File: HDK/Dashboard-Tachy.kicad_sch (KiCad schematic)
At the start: 54 parts, among them J101 Conn_02x08_Odd_Even, U101 CA56-12CGKWA

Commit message: updated rev1.1
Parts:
- H101, H102, H103, H104: footprint MountingHole:MountingHole_3.2mm_M3_DIN965_Pad_TopBottom -> MountingHole:MountingHole_4.3mm_M4_DIN965_Pad_TopBottom

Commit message: updated REV1.1
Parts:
- C101, C102, C103, C104, C105, C106, C107, C108, C109, C110, C111, C112, C113, C114, C115, C116, C117, C118, C119, C120, C121, C122, C123, C124: footprint Capacitor_SMD:C_0402_1005Metric -> Capacitor_SMD:C_0603_1608Metric; LCSC (none) -> C14663
- D101, D102, D103, D104, D105, D106, D107, D108, D109, D110, D111, D112, D113, D114, D115, D116, D117, D118, D119, D120, D121, D122, D123, D124: LCSC (none) -> C2761795

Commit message: added fab
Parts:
- D101, D102, D103, D104, D105, D106, D107, D108, D109, D110, D111, D112, D113, D114, D115, D116, D117, D118, D119, D120, D121, D122, D123, D124: LCSC C2761795 -> C2843785
- H101, H102, H103, H104: LCSC (none) -> -; now left out of the parts list
- J101: footprint Connector_JST:JST_PHD_B16B-PHDSS_2x08_P2.00mm_Vertical -> NVF-Kicad:PHD_02x08V-H; LCSC (none) -> -
- U101: LCSC (none) -> -

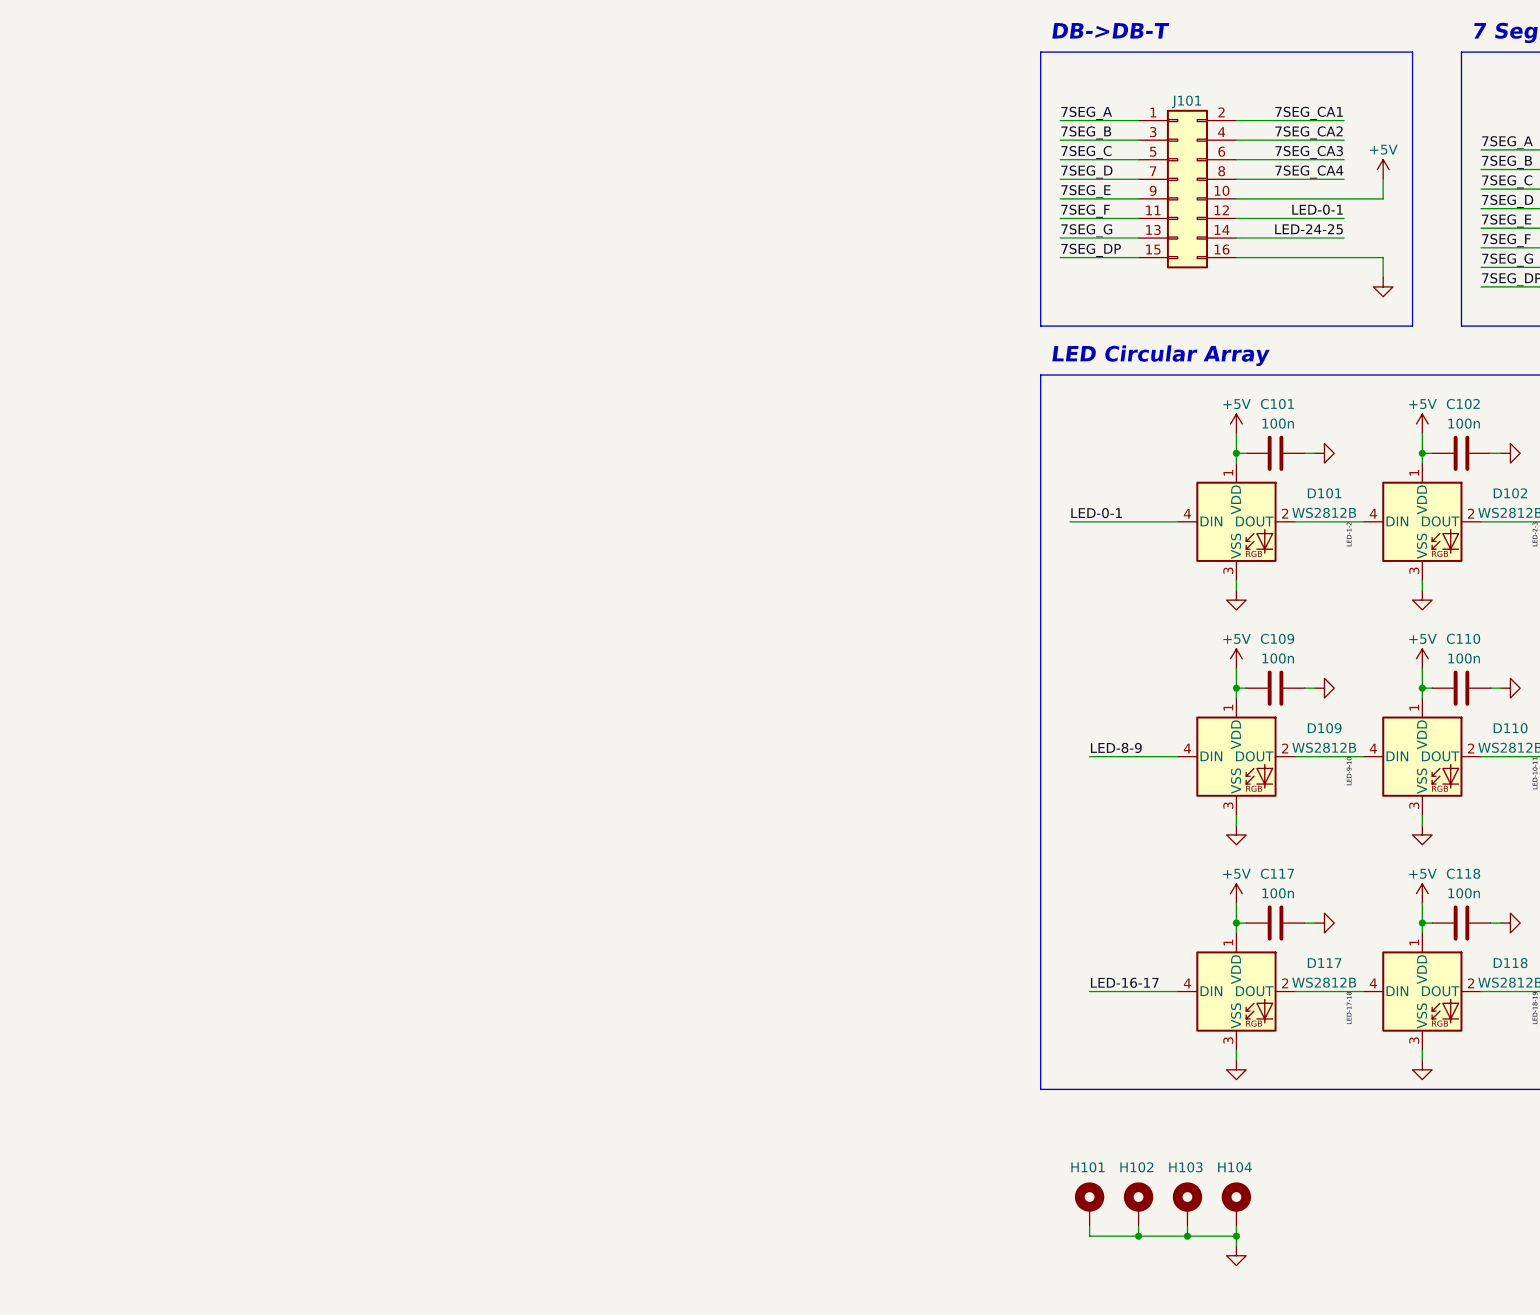
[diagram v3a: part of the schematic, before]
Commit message: updated dimensions
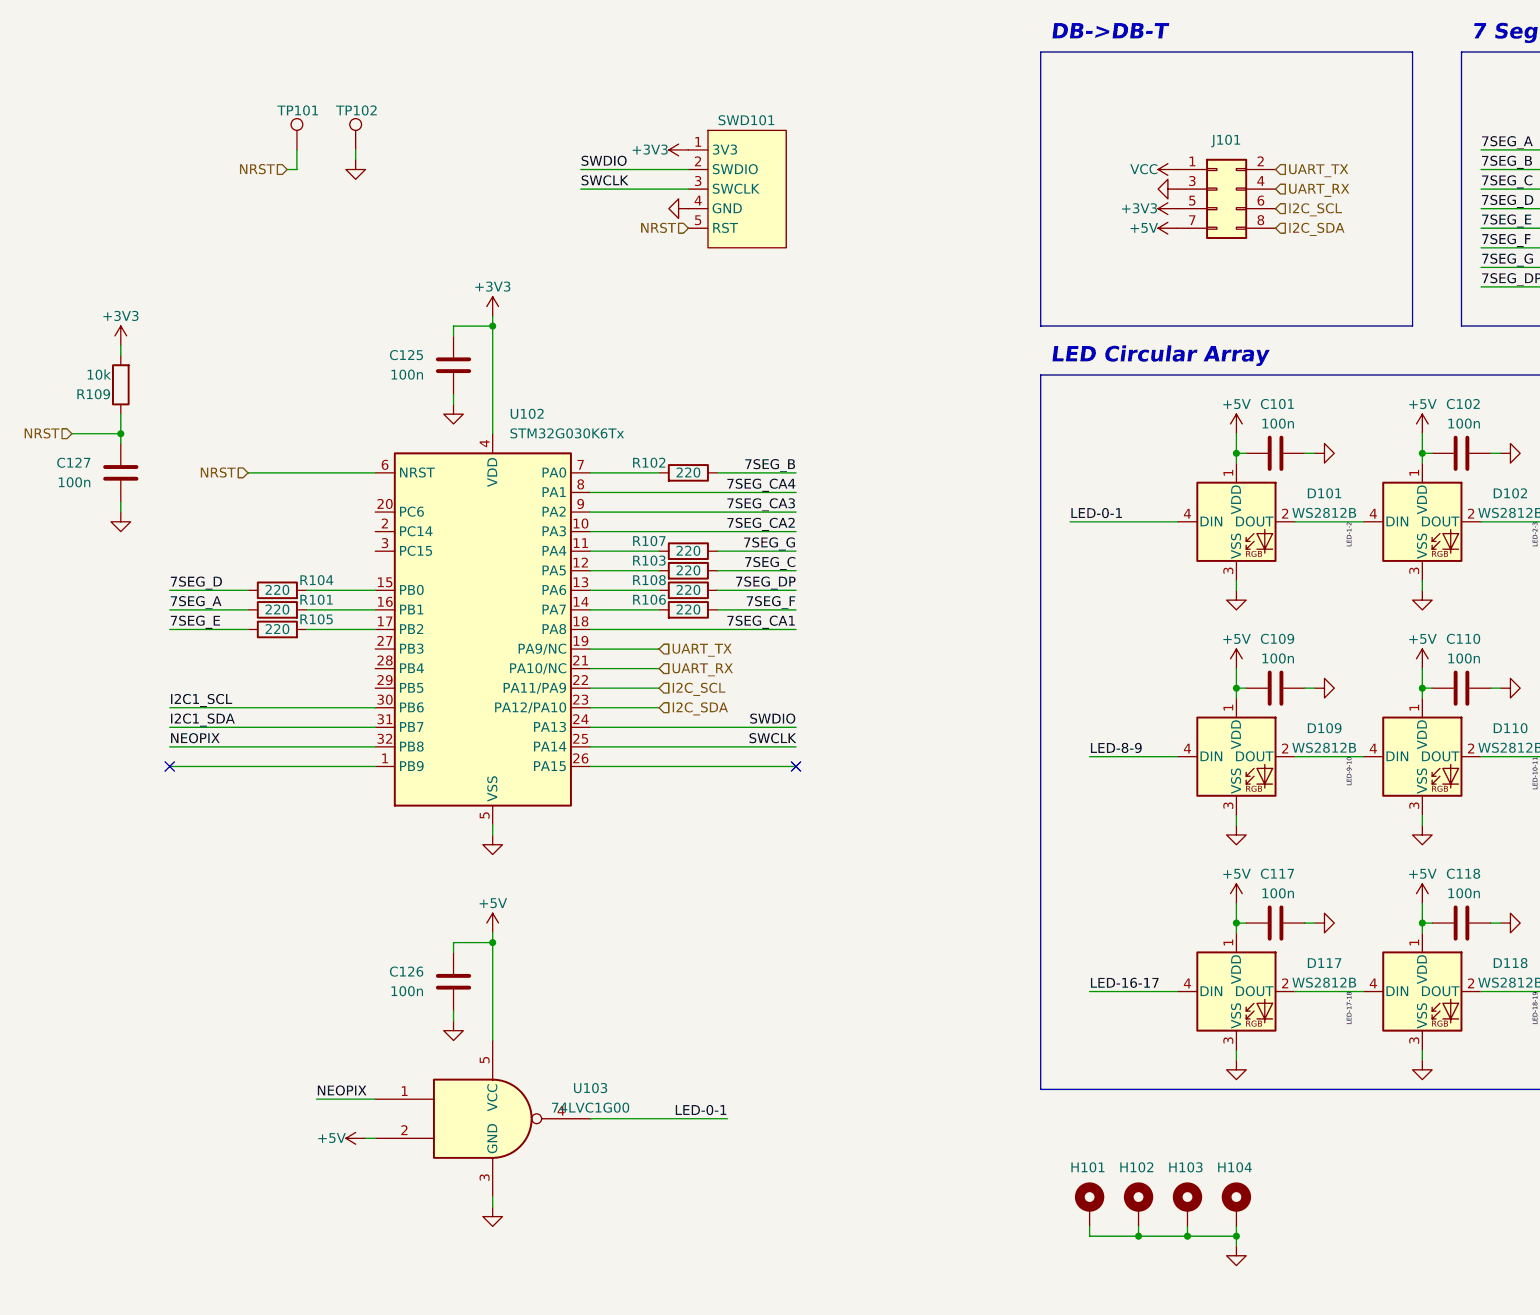
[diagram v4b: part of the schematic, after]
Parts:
- removed J101: Conn_02x08_Odd_Even, NVF-Kicad:PHD_02x08V-H, symbol Connector_Generic:Conn_02x08_Odd_Even
- added C125, C126, C127: 100n, Capacitor_SMD:C_0603_1608Metric, symbol Device:C
- added J101: Conn_02x04_Odd_Even, NVF-Kicad:PHD_02x04V-H, symbol Connector_Generic:Conn_02x04_Odd_Even
- added R101, R102, R103, R104, R105, R106, R107, R108: 220, Resistor_SMD:R_0603_1608Metric, symbol Device:R
- added R109: 10k, Resistor_SMD:R_0603_1608Metric, symbol Device:R
- added SWD101: SWD_Breakout_Minimal, NVF-Kicad:PH_01x05V-H, symbol NVF-Kicad:SWD_Breakout_Minimal
- added TP101, TP102: TestPoint, TestPoint:TestPoint_Pad_2.0x2.0mm, symbol Connector:TestPoint
- added U102: STM32G030K6Tx, Package_QFP:LQFP-32_7x7mm_P0.8mm, symbol MCU_ST_STM32G0:STM32G030K6Tx
- added U103: 74LVC1G00, Package_TO_SOT_SMD:SOT-23-5, symbol 74xGxx:74LVC1G00
- U101: footprint Display_7Segment:CA56-12CGKWA -> nvf:LDQ-M3604RI_LUM
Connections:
- net +5V: now also C126.2, J101.7 (Pin_7), U103.2, U103.5 (VCC)
- net 7SEG_A: now also R101.1
- net 7SEG_B: now also R102.1
- net 7SEG_C: now also R103.1
- net 7SEG_CA1: now also U102.18 (PA8)
- net 7SEG_CA2: now also U102.10 (PA3)
- net 7SEG_CA3: now also U102.9 (PA2)
- net 7SEG_CA4: now also U102.8 (PA1)
- net 7SEG_D: now also R104.1
- net 7SEG_DP: now also R108.1
- net 7SEG_E: now also R105.1
- net 7SEG_F: now also R106.1
- net 7SEG_G: now also R107.1
- net GND: now also C125.1, C126.1, C127.1, J101.3 (Pin_3), SWD101.4 (GND), TP102.1, U102.5 (VSS), U103.3 (GND)
- net LED-0-1: now also U103.4
- new net: R101.2, U102.16 (PB1)
- new net: R105.2, U102.17 (PB2)
- new net: R107.2, U102.11 (PA4)
- new net: R103.2, U102.12 (PA5)
- new net: R108.2, U102.13 (PA6)
- new net: R106.2, U102.14 (PA7)
- new net: R104.2, U102.15 (PB0)
- new net: R102.2, U102.7 (PA0)
- new net +3V3: C125.2, J101.5 (Pin_5), R109.2, SWD101.1 (3V3), U102.4 (VDD)
- new net I2C1_SCL: U102.30 (PB6)
- new net I2C1_SDA: U102.31 (PB7)
- new net I2C_SCL: J101.6 (Pin_6), U102.22 (PA11/PA9)
- new net I2C_SDA: J101.8 (Pin_8), U102.23 (PA12/PA10)
- new net NEOPIX: U102.32 (PB8), U103.1
- new net NRST: C127.2, R109.1, SWD101.5 (RST), TP101.1, U102.6 (NRST)
- new net SWCLK: SWD101.3 (SWCLK), U102.25 (PA14)
- new net SWDIO: SWD101.2 (SWDIO), U102.24 (PA13)
- new net UART_RX: J101.4 (Pin_4), U102.21 (PA10/NC)
- new net UART_TX: J101.2 (Pin_2), U102.19 (PA9/NC)
- new net VCC: J101.1 (Pin_1)
- no-connect marks 0 -> 2

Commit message: changed outline
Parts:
- J101, SWD101, TP101, TP102: LCSC (none) -> -
- R101, R102, R103, R104, R105, R106, R107, R108: LCSC (none) -> C22962
- R109: LCSC (none) -> C25804
- U101: value CA56-12CGKWA -> LDQ-M3604RI; footprint nvf:LDQ-M3604RI_LUM -> NVF-Kicad:04x7SegmentDispl
- U102: LCSC (none) -> C529331
- U103: LCSC (none) -> C434066
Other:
- moved on the sheet: C101, C102, C103, C104, C105, C106, C114, C115, C116, C125, C126, C127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
